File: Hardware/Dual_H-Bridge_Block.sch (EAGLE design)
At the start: 25 parts, among them U1 TB6612FNG, U2 EDISON_CONNECTOR_FULLMOUNTING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, U3 EDISON_CONNECTOR_FULLHEADER, U4 TXB0108

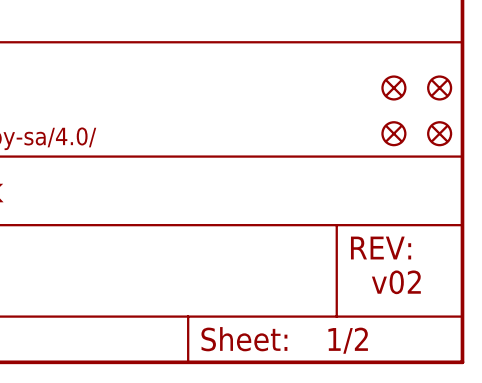
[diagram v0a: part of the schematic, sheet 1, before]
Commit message: corrected package footprint to remove bridging.
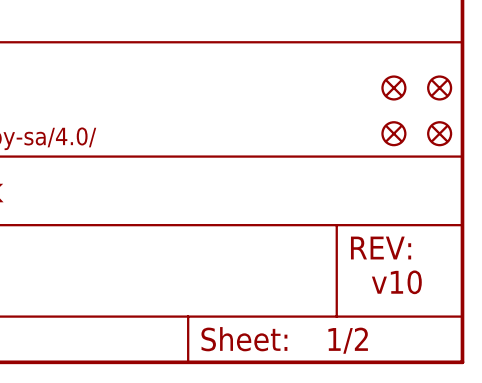
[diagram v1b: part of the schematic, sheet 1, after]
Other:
- note added: "v10"
- note removed: "v02"
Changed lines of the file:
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@@
 <?xml version="1.0" encoding="utf-8"?>
 <!DOCTYPE eagle SYSTEM "eagle.dtd">
-<eagle version="6.5.0">
+<eagle version="6.6.0">
 <drawing>
 <settings>
@@
 <sheet>
 <plain>
-<text x="238.76" y="7.62" size="2.54" layer="94">v02</text>
+<text x="238.76" y="7.62" size="2.54" layer="94">v10</text>
 <text x="167.64" y="10.16" size="2.54" layer="94">Casey Kuhns</text>
 <text x="93.98" y="55.88" size="1.27" layer="97">NOTE: Close this jumper to provide power to h-bridge using VSYS.

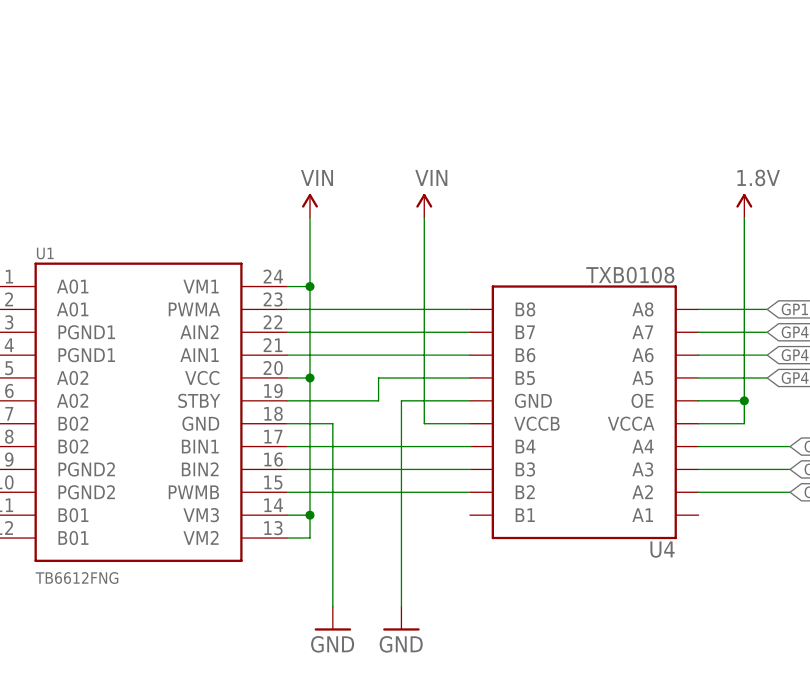
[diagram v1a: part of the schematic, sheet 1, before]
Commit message: Changed Logic to vsys from vin
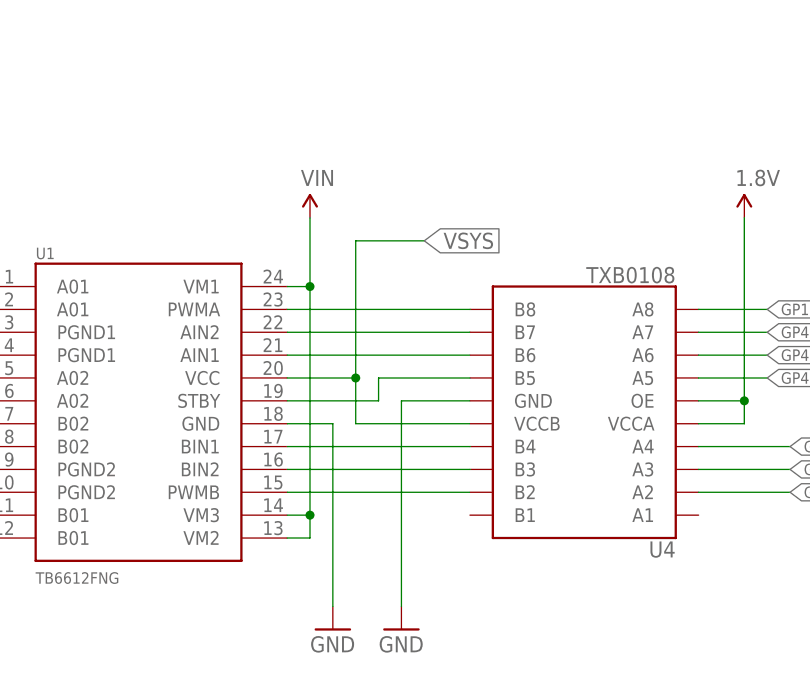
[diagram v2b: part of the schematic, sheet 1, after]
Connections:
- net VIN: no longer U1.VCC, U4.VCCB
- net VSYS: now also U1.VCC, U4.VCCB
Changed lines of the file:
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@@
 <layer number="255" name="routoute" color="7" fill="1" visible="yes" active="yes"/>
 </layers>
-<schematic xreflabel="%F%N/%S" xrefpart="1_/%S.%C%R">
+<schematic xreflabel="%F%N/%S" xrefpart="/%S.%C%R">
 <attributes>
 </attributes>
@@
 <part name="U4" library="Testing" deviceset="TXB0108" device=""/>
 <part name="GND6" library="SparkFun-Aesthetics" deviceset="GND" device=""/>
-<part name="SUPPLY3" library="SparkFun-Aesthetics" deviceset="VIN" device=""/>
 <part name="SUPPLY4" library="SparkFun-Aesthetics" deviceset="1.8V" device=""/>
 <part name="C1" library="SparkFun-Capacitors" deviceset="10UF-16V-10%(TANT)" device="" value="10uF"/>
@@
 <instance part="U4" gate="U1" x="167.64" y="106.68" rot="R180"/>
 <instance part="GND6" gate="1" x="147.32" y="83.82"/>
-<instance part="SUPPLY3" gate="G$1" x="149.86" y="129.54"/>
 <instance part="SUPPLY4" gate="G$1" x="185.42" y="129.54"/>
 <instance part="C1" gate="G$1" x="17.78" y="106.68"/>
@@
 <pinref part="U1" gate="G$1" pin="VM3"/>
 <wire x1="137.16" y1="96.52" x2="134.62" y2="96.52" width="0.1524" layer="91"/>
-<wire x1="137.16" y1="96.52" x2="137.16" y2="111.76" width="0.1524" layer="91"/>
+<wire x1="137.16" y1="96.52" x2="137.16" y2="121.92" width="0.1524" layer="91"/>
 <pinref part="U1" gate="G$1" pin="VM1"/>
-<wire x1="137.16" y1="111.76" x2="137.16" y2="121.92" width="0.1524" layer="91"/>
 <wire x1="137.16" y1="121.92" x2="134.62" y2="121.92" width="0.1524" layer="91"/>
 <junction x="137.16" y="96.52"/>
 <wire x1="137.16" y1="121.92" x2="137.16" y2="129.54" width="0.1524" layer="91"/>
 <junction x="137.16" y="121.92"/>
-<pinref part="U1" gate="G$1" pin="VCC"/>
-<wire x1="134.62" y1="111.76" x2="137.16" y2="111.76" width="0.1524" layer="91"/>
-<junction x="137.16" y="111.76"/>
 <pinref part="SUPPLY2" gate="G$1" pin="VIN"/>
-</segment>
-<segment>
-<wire x1="154.94" y1="106.68" x2="149.86" y2="106.68" width="0.1524" layer="91"/>
-<wire x1="149.86" y1="106.68" x2="149.86" y2="129.54" width="0.1524" layer="91"/>
-<pinref part="SUPPLY3" gate="G$1" pin="VIN"/>
-<pinref part="U4" gate="U1" pin="VCCB"/>
 </segment>
 <segment>
@@
 <label x="139.7" y="66.04" size="1.27" layer="95" xref="yes"/>
 </segment>
-</net>
+<segment>
+<pinref part="U4" gate="U1" pin="VCCB"/>
+<pinref part="U1" gate="G$1" pin="VCC"/>
+<wire x1="134.62" y1="111.76" x2="142.24" y2="111.76" width="0.1524" layer="91"/>
+<wire x1="142.24" y1="111.76" x2="142.24" y2="106.68" width="0.1524" layer="91"/>
+<wire x1="142.24" y1="106.68" x2="154.94" y2="106.68" width="0.1524" layer="91"/>
+<wire x1="142.24" y1="111.76" x2="142.24" y2="127" width="0.1524" layer="91"/>
+<junction x="142.24" y="111.76"/>
+<wire x1="142.24" y1="127" x2="149.86" y2="127" width="0.1524" layer="91"/>
+<label x="149.86" y="127" size="1.778" layer="95" xref="yes"/>
+</segment>
+</net>

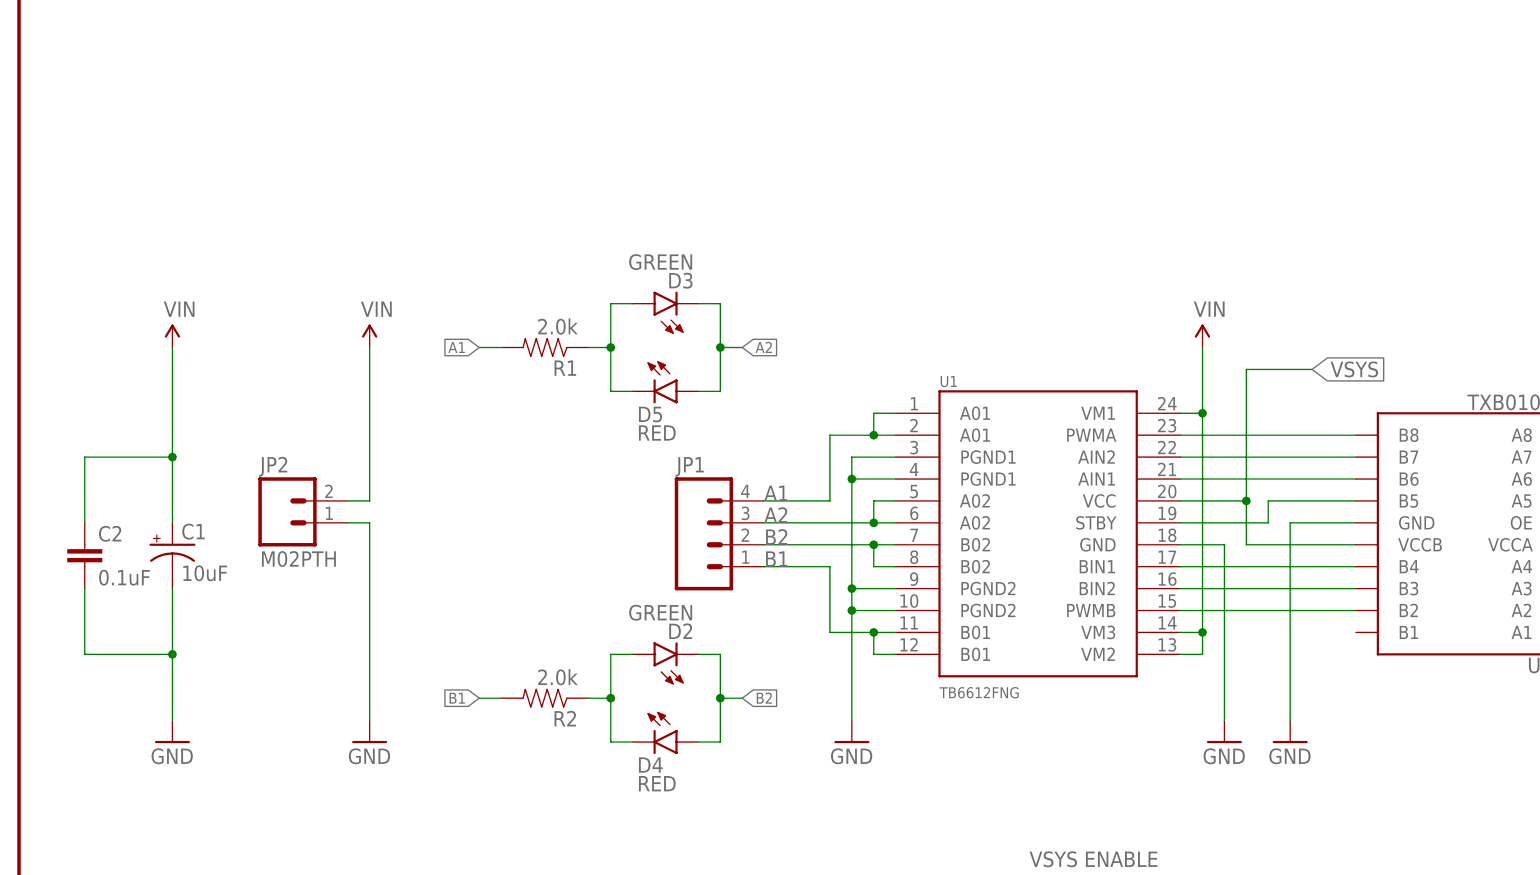
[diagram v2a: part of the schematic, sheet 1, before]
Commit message: finishing routing and cleaning up pads
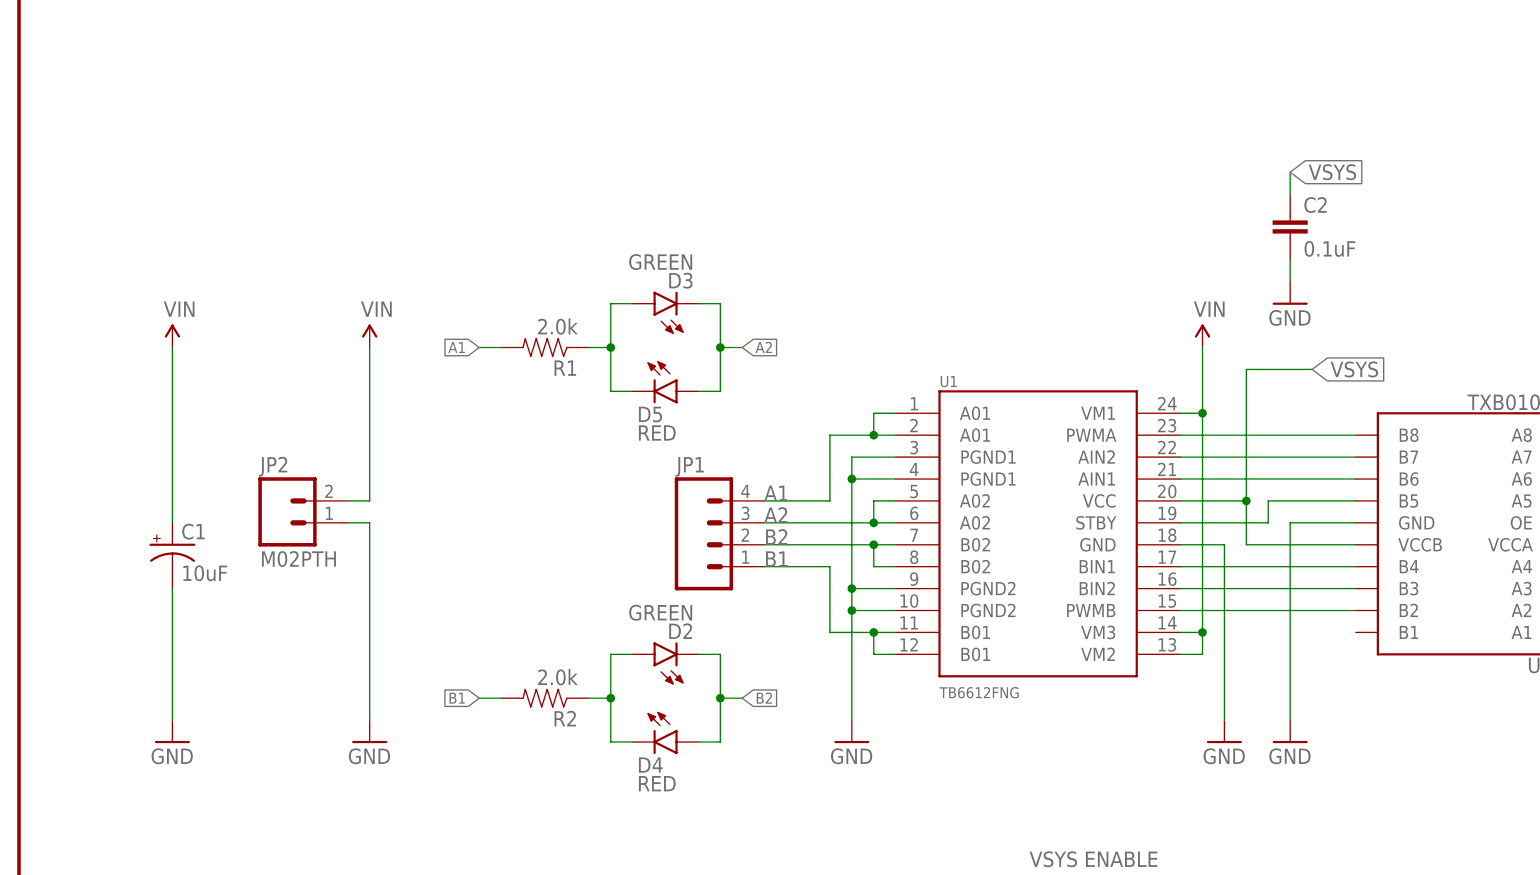
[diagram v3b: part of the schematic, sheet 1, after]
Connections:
- net VIN: no longer C2.1
- net VSYS: now also C2.1
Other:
- moved on the sheet: C2
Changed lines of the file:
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@@
 <part name="D4" library="SparkFun-LED" deviceset="LED-RED" device="0603" value="RED"/>
 <part name="D5" library="SparkFun-LED" deviceset="LED-RED" device="0603" value="RED"/>
+<part name="GND7" library="SparkFun-Aesthetics" deviceset="GND" device=""/>
 </parts>
 <sheets>
@@
 <instance part="SUPPLY4" gate="G$1" x="185.42" y="129.54"/>
 <instance part="C1" gate="G$1" x="17.78" y="106.68"/>
-<instance part="C2" gate="G$1" x="7.62" y="104.14"/>
+<instance part="C2" gate="G$1" x="147.32" y="142.24"/>
 <instance part="C3" gate="G$1" x="210.82" y="106.68"/>
 <instance part="SUPPLY5" gate="G$1" x="210.82" y="129.54"/>
@@
 <instance part="D4" gate="G$1" x="76.2" y="83.82" rot="R270"/>
 <instance part="D5" gate="G$1" x="76.2" y="124.46" rot="R270"/>
+<instance part="GND7" gate="1" x="147.32" y="134.62"/>
 </instances>
 <busses>
@@
 <segment>
 <pinref part="C1" gate="G$1" pin="-"/>
-<wire x1="17.78" y1="101.6" x2="17.78" y2="93.98" width="0.1524" layer="91"/>
-<wire x1="17.78" y1="93.98" x2="7.62" y2="93.98" width="0.1524" layer="91"/>
+<wire x1="17.78" y1="101.6" x2="17.78" y2="86.36" width="0.1524" layer="91"/>
+<pinref part="GND10" gate="1" pin="GND"/>
+</segment>
+<segment>
 <pinref part="C2" gate="G$1" pin="2"/>
-<wire x1="7.62" y1="93.98" x2="7.62" y2="101.6" width="0.1524" layer="91"/>
-<wire x1="17.78" y1="93.98" x2="17.78" y2="86.36" width="0.1524" layer="91"/>
-<pinref part="GND10" gate="1" pin="GND"/>
-<junction x="17.78" y="93.98"/>
+<pinref part="GND7" gate="1" pin="GND"/>
+<wire x1="147.32" y1="137.16" x2="147.32" y2="139.7" width="0.1524" layer="91"/>
 </segment>
 </net>
@@
 </segment>
 <segment>
-<pinref part="C2" gate="G$1" pin="1"/>
-<wire x1="7.62" y1="109.22" x2="7.62" y2="116.84" width="0.1524" layer="91"/>
-<wire x1="7.62" y1="116.84" x2="17.78" y2="116.84" width="0.1524" layer="91"/>
 <pinref part="C1" gate="G$1" pin="+"/>
-<wire x1="17.78" y1="116.84" x2="17.78" y2="109.22" width="0.1524" layer="91"/>
 <pinref part="SUPPLY6" gate="G$1" pin="VIN"/>
-<wire x1="17.78" y1="116.84" x2="17.78" y2="129.54" width="0.1524" layer="91"/>
-<junction x="17.78" y="116.84"/>
+<wire x1="17.78" y1="109.22" x2="17.78" y2="129.54" width="0.1524" layer="91"/>
 </segment>
 <segment>
@@
 <label x="149.86" y="127" size="1.778" layer="95" xref="yes"/>
 </segment>
-</net>
+<segment>
+<wire x1="147.32" y1="147.32" x2="147.32" y2="149.86" width="0.1524" layer="91"/>
+<pinref part="C2" gate="G$1" pin="1"/>
+<label x="147.32" y="149.86" size="1.778" layer="95" xref="yes"/>
+</segment>
+</net>

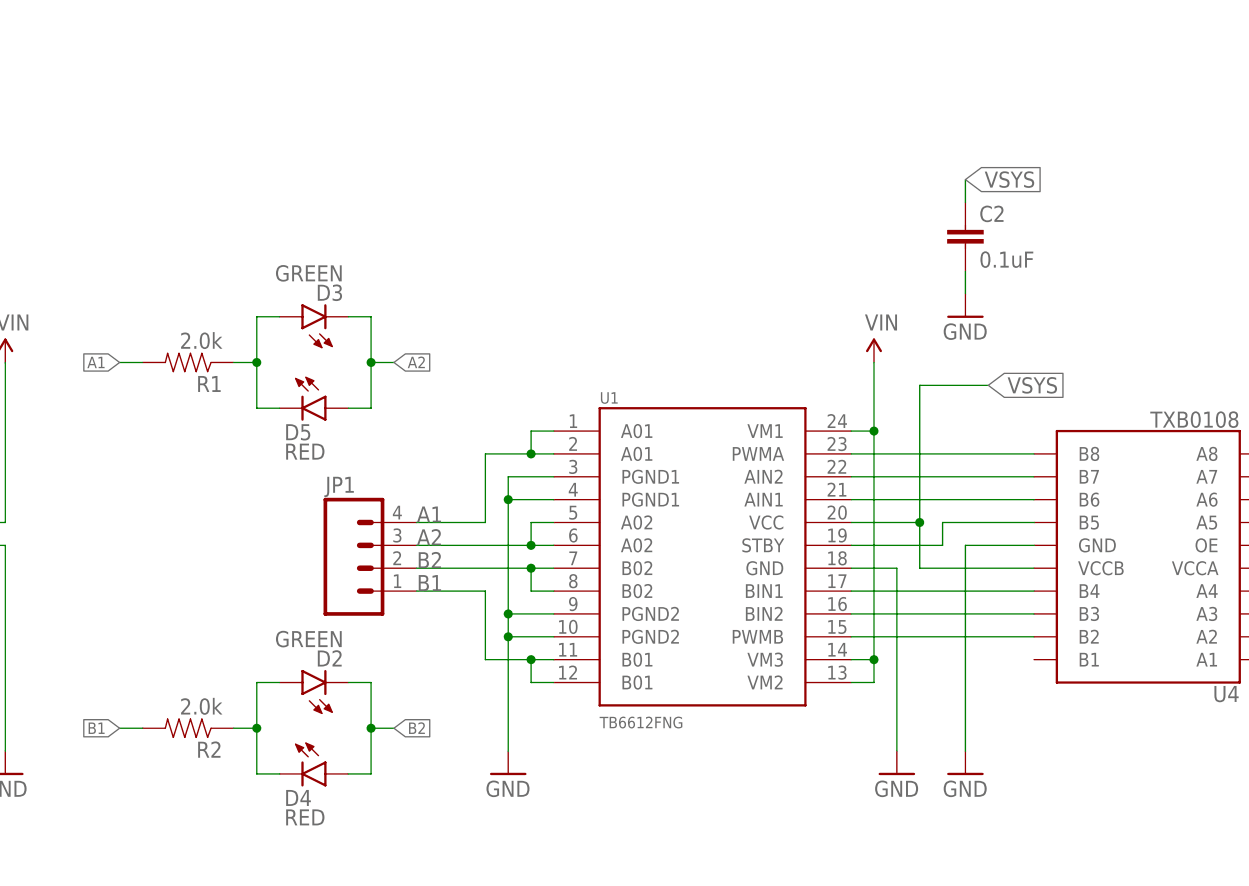
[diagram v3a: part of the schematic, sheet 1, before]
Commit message: Ready for reds. Change LED resistors to 680 ohm Thicken traces of drive Touch up schematic No known to-do items
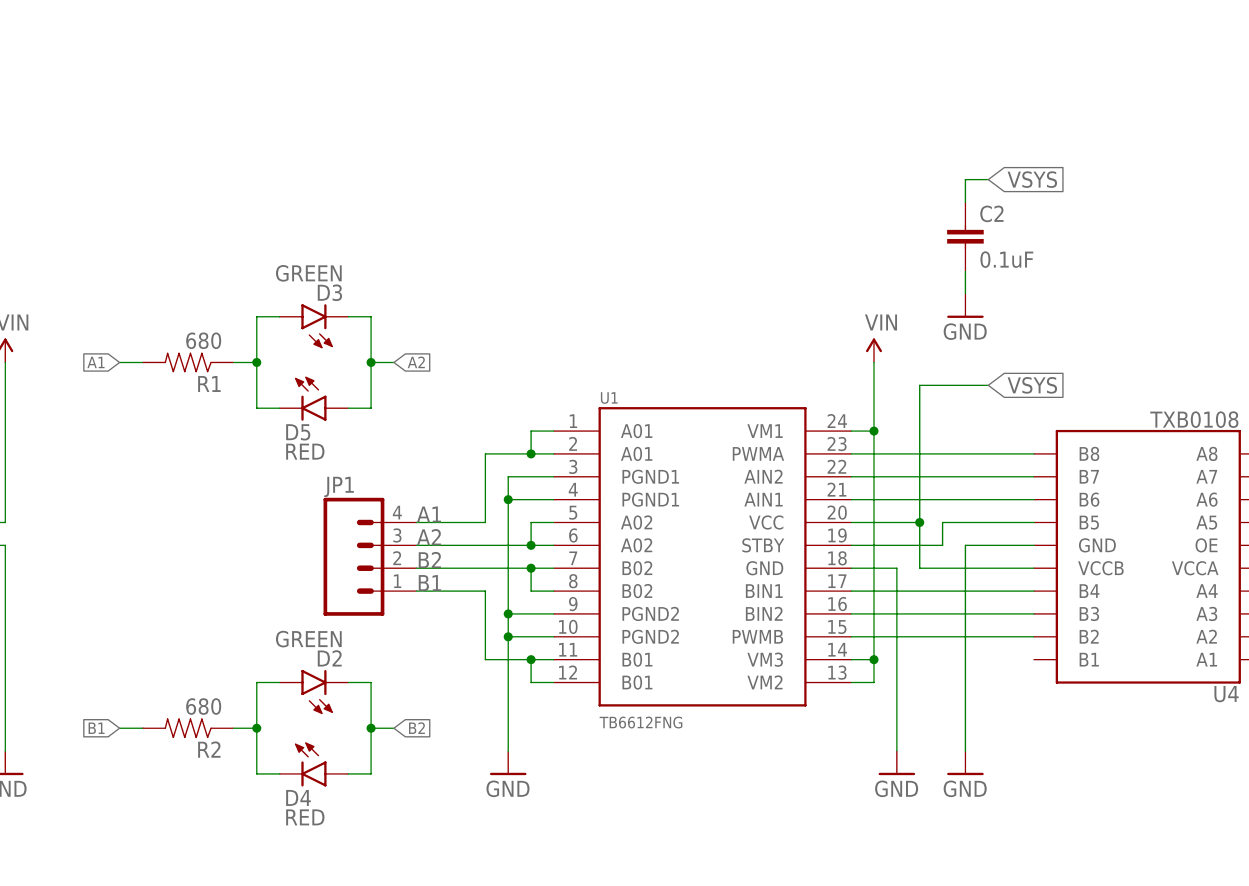
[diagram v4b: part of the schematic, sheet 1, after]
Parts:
- R1, R2: value 2.0k -> 680; device SparkFun-Resistors:2.0KOHM1/10W5%(0603) -> SparkFun-Resistors:680OHM1/10W5%(0603)
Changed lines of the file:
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@@
 <part name="SJ1" library="SparkFun-Passives" deviceset="JUMPER-PAD-2-NO" device="YES_SILK" value="VSYS ENABLE"/>
 <part name="D1" library="SparkFun-DiscreteSemi" deviceset="DIODE-SCHOTTKY" device="-MBRA140" value="MBRA140"/>
-<part name="R1" library="SparkFun-Resistors" deviceset="2.0KOHM1/10W5%(0603)" device="" value="2.0k"/>
-<part name="R2" library="SparkFun-Resistors" deviceset="2.0KOHM1/10W5%(0603)" device="" value="2.0k"/>
+<part name="R1" library="SparkFun-Resistors" deviceset="680OHM1/10W5%(0603)" device="" value="680"/>
+<part name="R2" library="SparkFun-Resistors" deviceset="680OHM1/10W5%(0603)" device="" value="680"/>
 <part name="D2" library="SparkFun-LED" deviceset="LED-GREEN" device="0603" value="GREEN"/>
 <part name="D3" library="SparkFun-LED" deviceset="LED-GREEN" device="0603" value="GREEN"/>
@@
 <segment>
 <wire x1="147.32" y1="147.32" x2="147.32" y2="149.86" width="0.1524" layer="91"/>
+<wire x1="147.32" y1="149.86" x2="149.86" y2="149.86" width="0.1524" layer="91"/>
 <pinref part="C2" gate="G$1" pin="1"/>
-<label x="147.32" y="149.86" size="1.778" layer="95" xref="yes"/>
-</segment>
-</net>
+<label x="149.86" y="149.86" size="1.778" layer="95" xref="yes"/>
+</segment>
+</net>
